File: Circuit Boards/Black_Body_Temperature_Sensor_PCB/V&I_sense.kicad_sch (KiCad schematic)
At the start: 0 parts

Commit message: Schematic ready for review
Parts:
- added R40, R45, R46: 10M, symbol Device:R
- added R41, R42, R43, R44: 50, symbol Device:R
- added U12: ADS131M04xPW, Package_SO:TSSOP-20_4.4x6.5mm_P0.65mm, symbol Analog_ADC:ADS131M04xPW
- added U13, U18: AD8421ARZ, symbol Amplifier_Instrumentation:AD8421ARZ
- added U14, U15, U16, U17, U19, U20, U21: OPA376xxDBV, Package_TO_SOT_SMD:SOT-23-5, symbol Amplifier_Operational:OPA376xxDBV
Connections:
- new net: R40.1, U16.1, U16.4 (-), U18.1 (-)
- new net: R42.1, U18.2 (Rg)
- new net: R42.2, U18.3 (Rg)
- new net: U17.1, U17.4 (-), U18.4 (+)
- new net: R43.1, U19.1, U19.4 (-)
- new net: R43.2, R44.1, U21.3 (+)
- new net: R41.1, U13.2 (Rg)
- new net: R41.2, U13.3 (Rg)
- new net: R46.1, U13.1 (-), U15.1, U15.4 (-)
- new net: U13.4 (+), U14.1, U14.4 (-)
- new net +3V3A: U12.1 (AVDD), U12.20 (DVDD), U13.8 (Vs+), U14.5 (V+), U15.5 (V+), U16.5 (V+), U17.5 (V+), U18.8 (Vs+), U19.5 (V+), U20.5 (V+), U21.5 (V+)
- new net -3V3A: U13.5 (Vs-), U14.2 (V-), U15.2 (V-), U16.2 (V-), U17.2 (V-), U18.5 (Vs-), U19.2 (V-), U20.2 (V-), U21.2 (V-)
- new net AIN0P: U12.3 (AIN0P), U13.7
- new net AIN1P: U12.6 (AIN1P), U18.7
- new net AIN2N: R45.1, U12.8 (AIN2N), U20.1, U20.4 (-)
- new net AIN2P: U12.7 (AIN2P), U21.1, U21.4 (-)
- new net GND: R40.2, R44.2, R45.2, R46.2, U12.19 (DGND), U12.2 (AGND), U12.4 (AIN0N), U12.5 (AIN1N), U13.6 (Ref), U18.6 (Ref)
- new net i_sense.I+: U17.3 (+)
- new net i_sense.I-: U16.3 (+)
- new net v_sense.V+: U14.3 (+), U19.3 (+)
- new net v_sense.V-: U15.3 (+), U20.3 (+)
- no-connect marks 0 -> 2

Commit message: Temperature Sensor Schematic Done, awaiting review
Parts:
- added U22: ISO7762FDBQ, Package_SO:SSOP-16_3.9x4.9mm_P0.635mm, symbol Isolator:ISO7762FDBQ
- R43, R44: value 50 -> 10k
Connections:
- net +3V3A: now also U22.16 (Vcc2)
- net GND: now also U22.9 (GND2)
- net at U12.12 (~{CS}): now also U22.12 (OUTD)
- net at U12.13 (~{DRDY}): now also U22.10 (INF)
- net at U12.14 (SCLK): now also U22.14 (OUTB)
- net at U12.15 (DOUT): now also U22.11 (INE)
- net at U12.16 (DIN): now also U22.13 (OUTC)
- net at U12.17 (CLKIN): now also U22.15 (OUTA)
- new net +3V3: U22.1 (Vcc1)
- new net ADC_DRDY: U22.7 (OUTF)
- new net CLK_MCO: U22.2 (INA)
- new net GNDPWR: U22.8 (GND1)
- new net SPI.CS: U22.5 (IND)
- new net SPI.MISO: U22.6 (OUTE)
- new net SPI.MOSI: U22.4 (INC)
- new net SPI.SCLK: U22.3 (INB)

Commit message: Temp sensor schematic done
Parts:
- removed U13: AD8421ARZ, symbol Amplifier_Instrumentation:AD8421ARZ
- added U505: AD8421ARZ, Package_SO:SOIC-8_3.9x4.9mm_P1.27mm, symbol Amplifier_Instrumentation:AD8421ARZ
- R501: renamed from R41; footprint (none) -> Resistor_SMD:R_0603_1608Metric
- R502: renamed from R46; footprint (none) -> Resistor_SMD:R_0603_1608Metric
- R503: renamed from R42; footprint (none) -> Resistor_SMD:R_0603_1608Metric
- R504: renamed from R40; footprint (none) -> Resistor_SMD:R_0603_1608Metric
- R505: renamed from R43; footprint (none) -> Resistor_SMD:R_0603_1608Metric
- R506: renamed from R44; footprint (none) -> Resistor_SMD:R_0603_1608Metric
- R507: renamed from R45; footprint (none) -> Resistor_SMD:R_0603_1608Metric
- U506: renamed from U18; footprint (none) -> Package_SO:SOIC-8_3.9x4.9mm_P1.27mm
- renumbered U15 to U501, U14 to U502, U16 to U503, U17 to U504, U12 to U507, U19 to U508, U20 to U509, U21 to U510, U22 to U511
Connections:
- net +3V3A: now also U505.8 (Vs+)
- net -3V3A: now also U505.5 (Vs-)
- net AIN0P: now also U505.7
- net GND: now also U505.6 (Ref)
- net at R501.1: now also U505.2 (Rg)
- net at R501.2: now also U505.3 (Rg)
- net at R502.1, U501.1, U501.4 (-): now also U505.1 (-)
- net at U502.1, U502.4 (-): now also U505.4 (+)
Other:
- note added: "V/I Sense (PAGE 5)"
- moved on the sheet: R501, R502, U501, U502

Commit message: temp pcb analog layout done
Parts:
- removed R507: 10M, Resistor_SMD:R_0603_1608Metric, symbol Device:R
- removed U508, U509: OPA376xxDBV, Package_TO_SOT_SMD:SOT-23-5, symbol Amplifier_Operational:OPA376xxDBV
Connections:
- net AIN2N: now also R502.1, U501.1, U501.4 (-), U505.1 (-)
- net sense_iso_V+: now reaches U502.1, U502.4 (-), U505.4 (+)
- net sense_iso_V+: now also R505.1

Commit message: Digital section done
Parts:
- added C501: 220nf, Capacitor_SMD:C_0603_1608Metric, symbol Device:C
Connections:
- net AIN0P: now also U506.7; no longer U505.7
- net AIN1P: now also U505.7; no longer U506.7
- net GND: now also C501.2
- net cap: now reaches U507.18 (CAP)
- net cap: now also C501.1
- net AIN2N renamed sense_iso_V-
- no-connect marks 2 -> 3
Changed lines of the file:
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@@
 	)
 	(junction
+		(at 168.91 73.66)
+		(diameter 0)
+		(color 0 0 0 0)
+	)
+	(junction
 		(at 88.9 127)
 		(diameter 0)
@@
 	)
 	(junction
-		(at 158.75 72.39)
+		(at 101.6 81.28)
 		(diameter 0)
 		(color 0 0 0 0)
 	)
 	(junction
-		(at 101.6 81.28)
+		(at 78.74 53.34)
 		(diameter 0)
 		(color 0 0 0 0)
 	)
 	(junction
-		(at 78.74 53.34)
+		(at 105.41 154.94)
 		(diameter 0)
 		(color 0 0 0 0)
 	)
 	(junction
-		(at 105.41 154.94)
+		(at 161.29 73.66)
 		(diameter 0)
 		(color 0 0 0 0)
@@
 		(at 146.05 64.77)
 	)
+	(no_connect
+		(at 176.53 59.69)
+	)
 	(bus_entry
 		(at 245.11 49.53)
@@
 	(wire
 		(pts
-			(xy 138.43 54.61) (xy 146.05 54.61)
+			(xy 133.35 54.61) (xy 146.05 54.61)
 		)
 		(stroke
@@
 	(wire
 		(pts
-			(xy 138.43 57.15) (xy 146.05 57.15)
+			(xy 133.35 57.15) (xy 146.05 57.15)
 		)
 		(stroke
@@
 	(wire
 		(pts
-			(xy 138.43 39.37) (xy 146.05 39.37)
+			(xy 133.35 39.37) (xy 146.05 39.37)
 		)
 		(stroke
@@
 	(wire
 		(pts
+			(xy 179.07 64.77) (xy 176.53 64.77)
+		)
+		(stroke
+			(width 0)
+			(type default)
+		)
+	)
+	(wire
+		(pts
 			(xy 82.55 127) (xy 80.01 127)
 		)
@@
 	(wire
 		(pts
-			(xy 138.43 49.53) (xy 146.05 49.53)
+			(xy 133.35 49.53) (xy 146.05 49.53)
 		)
 		(stroke
@@
 	(wire
 		(pts
+			(xy 158.75 73.66) (xy 168.91 73.66)
+		)
+		(stroke
+			(width 0)
+			(type default)
+		)
+	)
+	(wire
+		(pts
 			(xy 163.83 34.29) (xy 163.83 31.75)
 		)
@@
 	(wire
 		(pts
-			(xy 138.43 41.91) (xy 146.05 41.91)
+			(xy 133.35 41.91) (xy 146.05 41.91)
 		)
 		(stroke
@@
 	(wire
 		(pts
-			(xy 138.43 46.99) (xy 146.05 46.99)
+			(xy 168.91 73.66) (xy 179.07 73.66)
 		)
 		(stroke
@@
 	(wire
 		(pts
-			(xy 214.63 33.02) (xy 214.63 34.29)
+			(xy 133.35 46.99) (xy 146.05 46.99)
 		)
 		(stroke
@@
 	(wire
 		(pts
-			(xy 161.29 72.39) (xy 158.75 72.39)
+			(xy 214.63 33.02) (xy 214.63 34.29)
 		)
 		(stroke
@@
 	(wire
 		(pts
-			(xy 158.75 72.39) (xy 158.75 69.85)
+			(xy 158.75 73.66) (xy 158.75 69.85)
 		)
 		(stroke
@@
 	(wire
 		(pts
-			(xy 161.29 69.85) (xy 161.29 72.39)
+			(xy 161.29 69.85) (xy 161.29 73.66)
 		)
 		(stroke
@@
 	(wire
 		(pts
-			(xy 177.8 137.16) (xy 218.44 137.16)
+			(xy 179.07 66.04) (xy 179.07 64.77)
 		)
 		(stroke
@@
 		)
 	)
-	(label "AIN0N"
+	(label "AIN1N"
 		(at 116.84 81.28 180)
 		(effects
@@
 		)
 	)
-	(label "sense_iso_V-"
-		(at 177.8 137.16 0)
-		(effects
-			(font
-				(size 1.27 1.27)
-			)
-			(justify left bottom)
-		)
-	)
 	(label "SPI.MOSI"
 		(at 222.25 49.53 0)
@@
 	)
 	(label "AIN0N"
-		(at 138.43 41.91 0)
+		(at 133.35 41.91 0)
 		(effects
 			(font
@@
 	)
 	(label "AIN1N"
-		(at 138.43 49.53 0)
+		(at 133.35 49.53 0)
 		(effects
 			(font
@@
 		)
 	)
-	(label "AIN2N"
-		(at 218.44 137.16 180)
-		(effects
-			(font
-				(size 1.27 1.27)
-			)
-			(justify right bottom)
-		)
-	)
 	(label "i_sense.I+"
 		(at 44.45 162.56 0)
@@
 		)
 	)
-	(label "AIN2N"
-		(at 138.43 57.15 0)
+	(label "v_sense.V-"
+		(at 45.72 50.8 0)
 		(effects
 			(font
@@
 		)
 	)
-	(label "v_sense.V-"
-		(at 45.72 50.8 0)
+	(label "cap"
+		(at 176.53 64.77 0)
 		(effects
 			(font
@@
 	)
 	(label "AIN0P"
-		(at 138.43 39.37 0)
+		(at 133.35 39.37 0)
 		(effects
 			(font
@@
 		)
 	)
-	(label "AIN1P"
+	(label "AIN0P"
 		(at 119.38 147.32 180)
 		(effects
@@
 		)
 	)
-	(label "AIN0P"
+	(label "AIN1P"
 		(at 116.84 73.66 180)
 		(effects
@@
 		)
 	)
+	(label "sense_iso_V-"
+		(at 133.35 57.15 0)
+		(effects
+			(font
+				(size 1.27 1.27)
+			)
+			(justify left bottom)
+		)
+	)
 	(label "SPI.MISO"
 		(at 222.25 54.61 0)
@@
 	)
 	(label "AIN2P"
-		(at 138.43 54.61 0)
+		(at 133.35 54.61 0)
 		(effects
 			(font
@@
 		)
 	)
-	(label "AIN1N"
+	(label "AIN0N"
 		(at 119.38 154.94 180)
 		(effects
@@
 	)
 	(label "AIN1P"
-		(at 138.43 46.99 0)
+		(at 133.35 46.99 0)
 		(effects
 			(font
@@
 	)
 	(symbol
+		(lib_id "Device:C")
+		(at 179.07 69.85 0)
+		(mirror y)
+		(unit 1)
+		(body_style 1)
+		(exclude_from_sim no)
+		(in_bom yes)
+		(on_board yes)
+		(in_pos_files yes)
+		(dnp no)
+		(property "Reference" "C501"
+			(at 176.53 68.58 0)
+			(show_name no)
+			(do_not_autoplace no)
+			(effects
+				(font
+					(size 1.27 1.27)
+				)
+				(justify left)
+			)
+		)
+		(property "Value" "220nf"
+			(at 176.53 71.12 0)
+			(show_name no)
+			(do_not_autoplace no)
+			(effects
+				(font
+					(size 1.27 1.27)
+				)
+				(justify left)
+			)
+		)
+		(property "Footprint" "Capacitor_SMD:C_0603_1608Metric"
+			(at 178.1048 73.66 0)
+			(hide yes)
+			(show_name no)
+			(do_not_autoplace no)
+			(effects
+				(font
+					(size 1.27 1.27)
+				)
+			)
+		)
+		(property "Datasheet" ""
+			(at 179.07 69.85 0)
+			(hide yes)
+			(show_name no)
+			(do_not_autoplace no)
+			(effects
+				(font
+					(size 1.27 1.27)
+				)
+			)
+		)
+		(property "Description" "Unpolarized capacitor"
+			(at 179.07 69.85 0)
+			(hide yes)
+			(show_name no)
+			(do_not_autoplace no)
+			(effects
+				(font
+					(size 1.27 1.27)
+				)
+			)
+		)
+		(pin "1"
+		)
+		(pin "2"
+		)
+		(instances
+			(project "Black_Body_Temperature_Sensor_PCB"
+				(path "/e46fba8d-0294-4f4f-927d-8614bb9d51d3/497ae29c-3205-4255-92aa-23b986f138da"
+					(reference "C501")
+					(unit 1)
+				)
+			)
+		)
+	)
+	(symbol
 		(lib_id "power:+4V")
 		(at 93.98 83.82 180)
@@
 	(symbol
 		(lib_id "power:GND")
-		(at 158.75 72.39 0)
+		(at 168.91 73.66 0)
 		(unit 1)
 		(body_style 1)
@@
 		(fields_autoplaced yes)
 		(property "Reference" "#PWR0517"
-			(at 158.75 78.74 0)
+			(at 168.91 80.01 0)
 			(hide yes)
 			(show_name no)
@@
 		)
 		(property "Value" "GND"
-			(at 158.75 77.47 0)
+			(at 168.91 78.74 0)
 			(show_name no)
 			(do_not_autoplace no)
@@
 		)
 		(property "Footprint" ""
-			(at 158.75 72.39 0)
+			(at 168.91 73.66 0)
 			(hide yes)
 			(show_name no)
@@
 		)
 		(property "Datasheet" ""
-			(at 158.75 72.39 0)
+			(at 168.91 73.66 0)
 			(hide yes)
 			(show_name no)
@@
 		)
 		(property "Description" "Power symbol creates a global label with name \"GND\" , ground"
-			(at 158.75 72.39 0)
+			(at 168.91 73.66 0)
 			(hide yes)
 			(show_name no)

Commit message: Complete except for recommended changes
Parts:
- renumbered U511 to U508, U510 to U509
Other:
- note added: "Temp sensor resistances"
- moved on the sheet: C501, R505, R506, U507, U508, U509

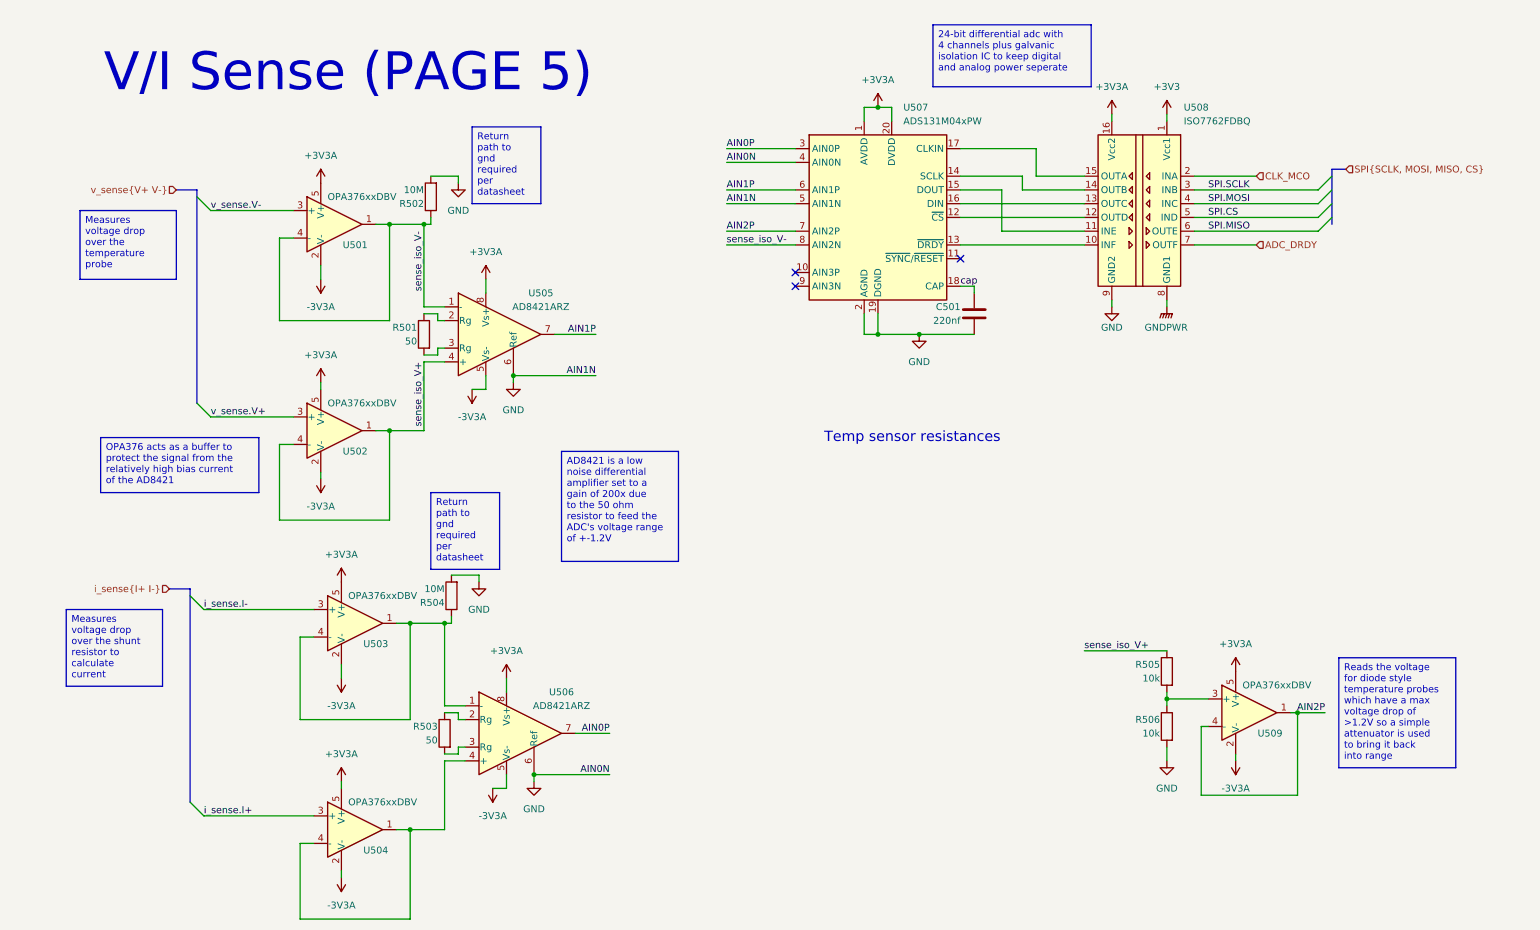
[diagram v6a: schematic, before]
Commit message: Temp probe bom done
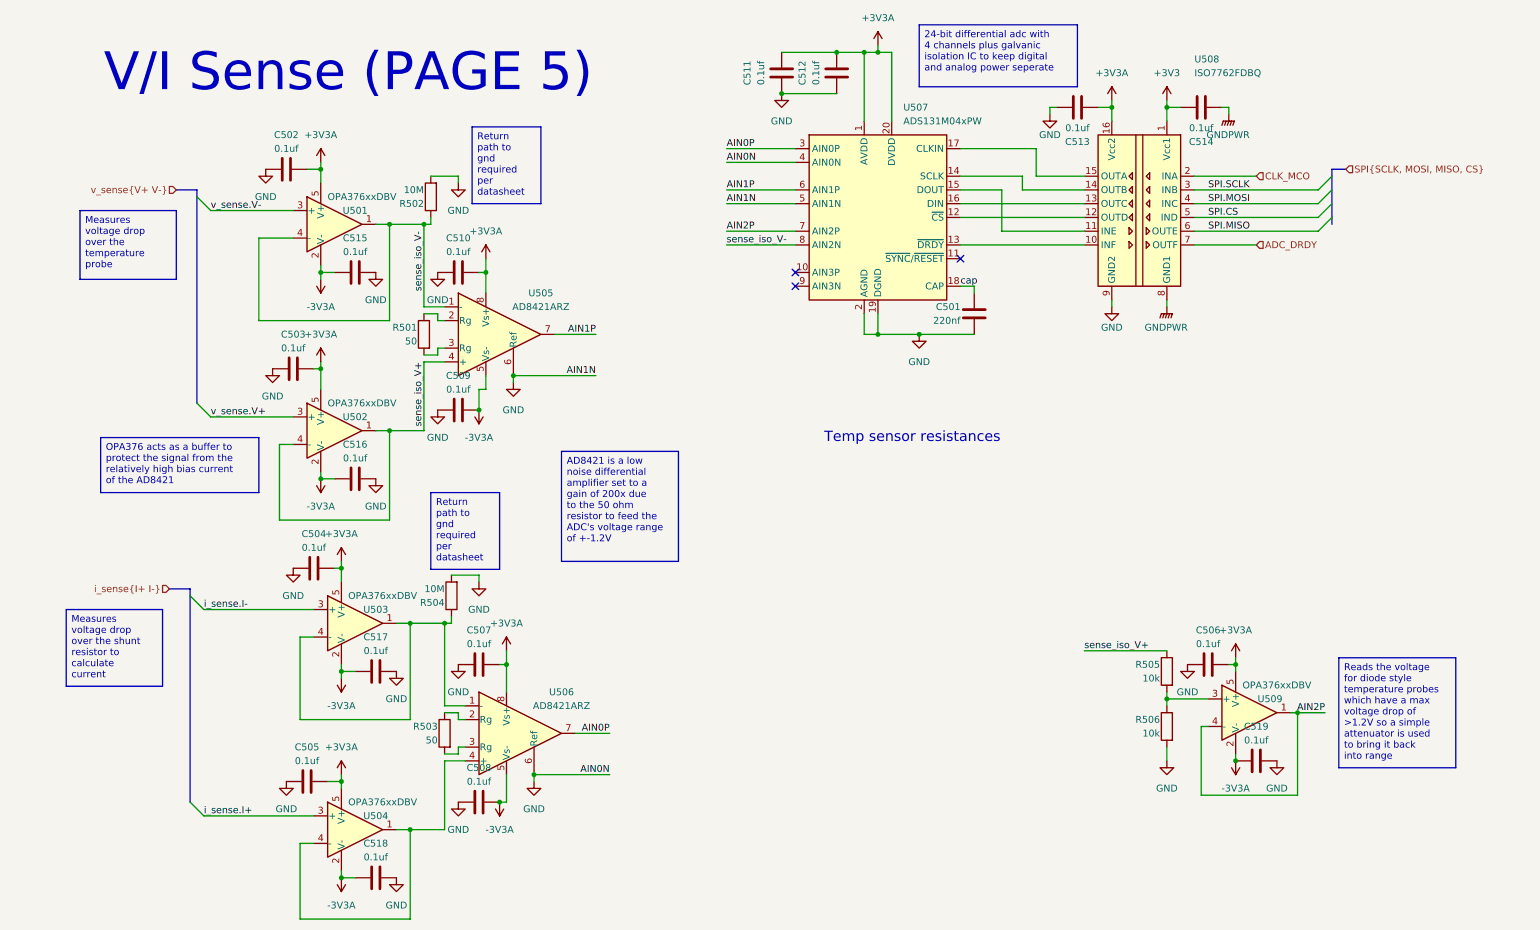
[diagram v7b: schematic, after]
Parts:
- added C502, C503, C504, C505, C506, C507, C508, C509, C510, C511, C512, C513, C514, C515, C516, C517, C518, C519: 0.1uf, Capacitor_SMD:C_0603_1608Metric, symbol Device:C
- C501: MPN (none) -> GCM188R71H224KA64D
- R501, R503: MPN (none) -> ERA-3AEB49R9V
- R502, R504: MPN (none) -> CRCW060310M0DHEAP
- R505, R506: MPN (none) -> ERA-3AEB103V
- U501, U502, U503, U504, U509: MPN (none) -> OPA376AIDBVR
- U505, U506: MPN (none) -> AD8421ARZ
- U507: MPN (none) -> ADS131M04IPWR
- U508: MPN (none) -> ISO7762FDBQ
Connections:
- net +3V3: now also C514.2
- net +3V3A: now also C502.1, C503.1, C504.1, C505.1, C506.1, C507.1, C510.1, C511.1, C512.1, C513.2
- net -3V3A: now also C508.1, C509.1, C515.1, C516.1, C517.1, C518.1, C519.1
- net GND: now also C502.2, C503.2, C504.2, C505.2, C506.2, C507.2, C508.2, C509.2, C510.2, C511.2, C512.2, C513.1, C515.2, C516.2, C517.2, C518.2, C519.2
- net GNDPWR: now also C514.1
